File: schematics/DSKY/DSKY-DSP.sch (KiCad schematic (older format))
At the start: 0 parts

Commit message: Add files via upload
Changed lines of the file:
@@
 Wire Bus Line
 	5000 3600 5850 3600
-Wire Wire Line
-	7200 4950 8450 4950
 Wire Bus Line
 	2950 3900 3950 3900
@@
 F9 "DA2[1..3]" I L 8450 2150 50
 F10 "DA3[1..3]" I L 8450 2300 50
-F11 "MODE1" I L 8450 4950 50
-F12 "ID2[0..4]" I L 8450 4650 50
-F13 "ID3[0..4]" I L 8450 4800 50
+F11 "ID2[0..4]" I L 8450 4650 50
+F12 "ID3[0..4]" I L 8450 4800 50
 $EndSheet
 $Sheet
@@
 F4 "WRITE1" O R 7200 5050 50
 F5 "RWD[0..12]" I R 7200 4150 50
-F6 "MODE1" O R 7200 4950 50
-F7 "OW[11..11]" I L 5850 4050 50
-F8 "ID2[0..4]" O R 7200 4650 50
-F9 "ID3[0..4]" O R 7200 4800 50
-F10 "BI[1..8]" I L 5850 4250 50
+F6 "OW[11..11]" I L 5850 4050 50
+F7 "ID2[0..4]" O R 7200 4650 50
+F8 "ID3[0..4]" O R 7200 4800 50
+F9 "BI[1..8]" I L 5850 4250 50
 $EndSheet
 Wire Bus Line

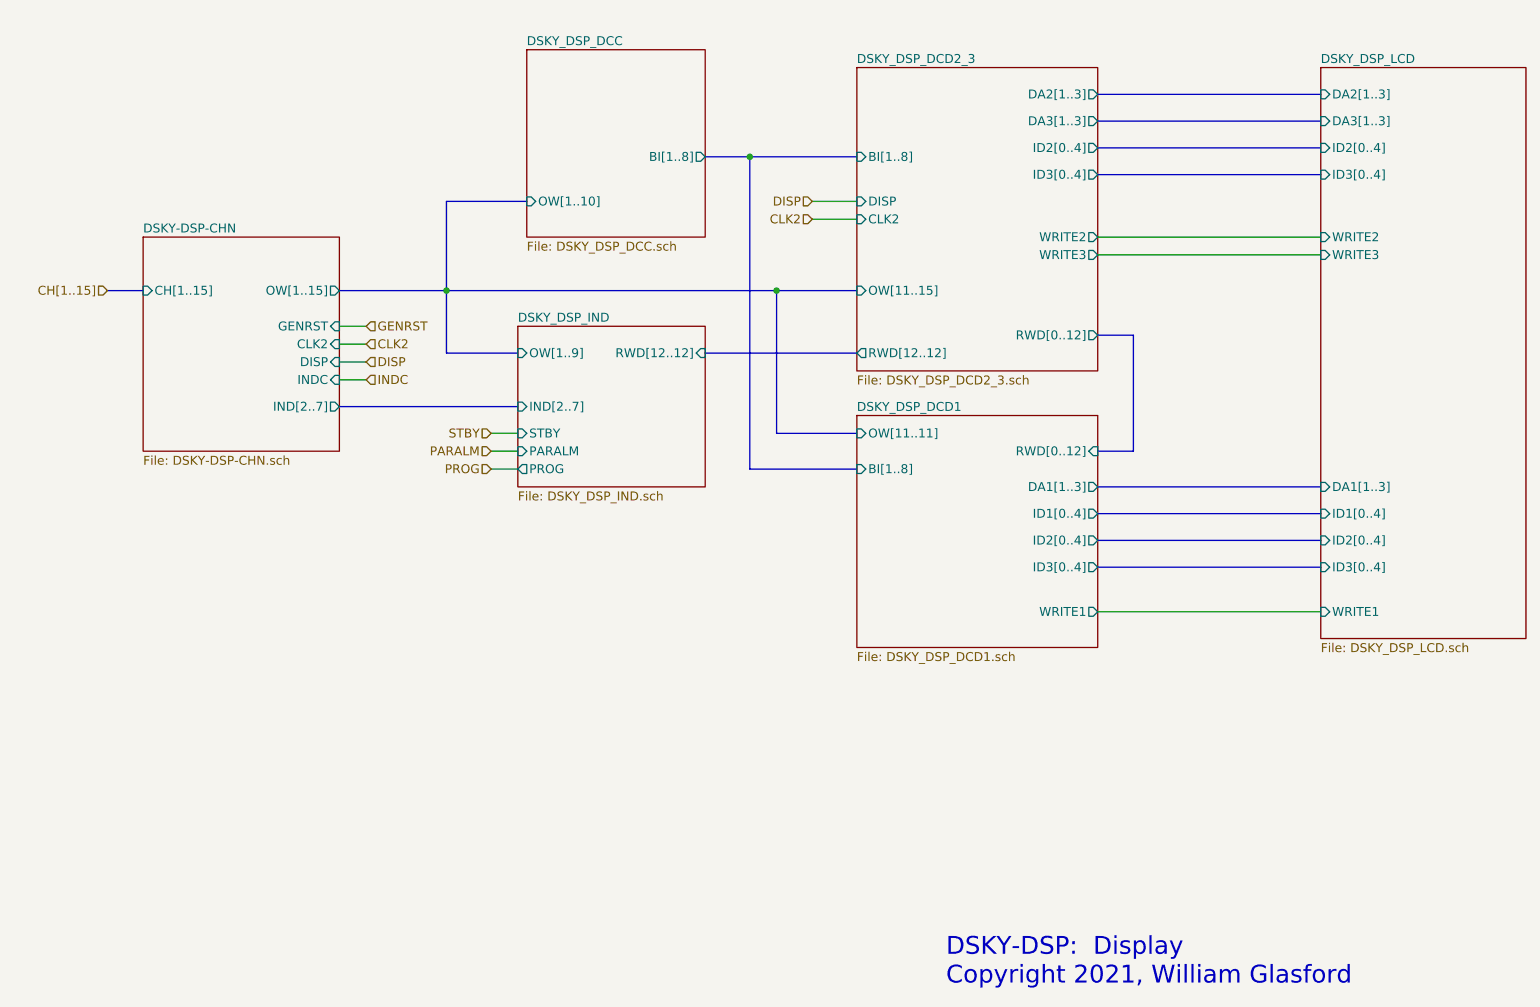
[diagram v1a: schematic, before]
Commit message: Minor tweaks to the display decoding logic.
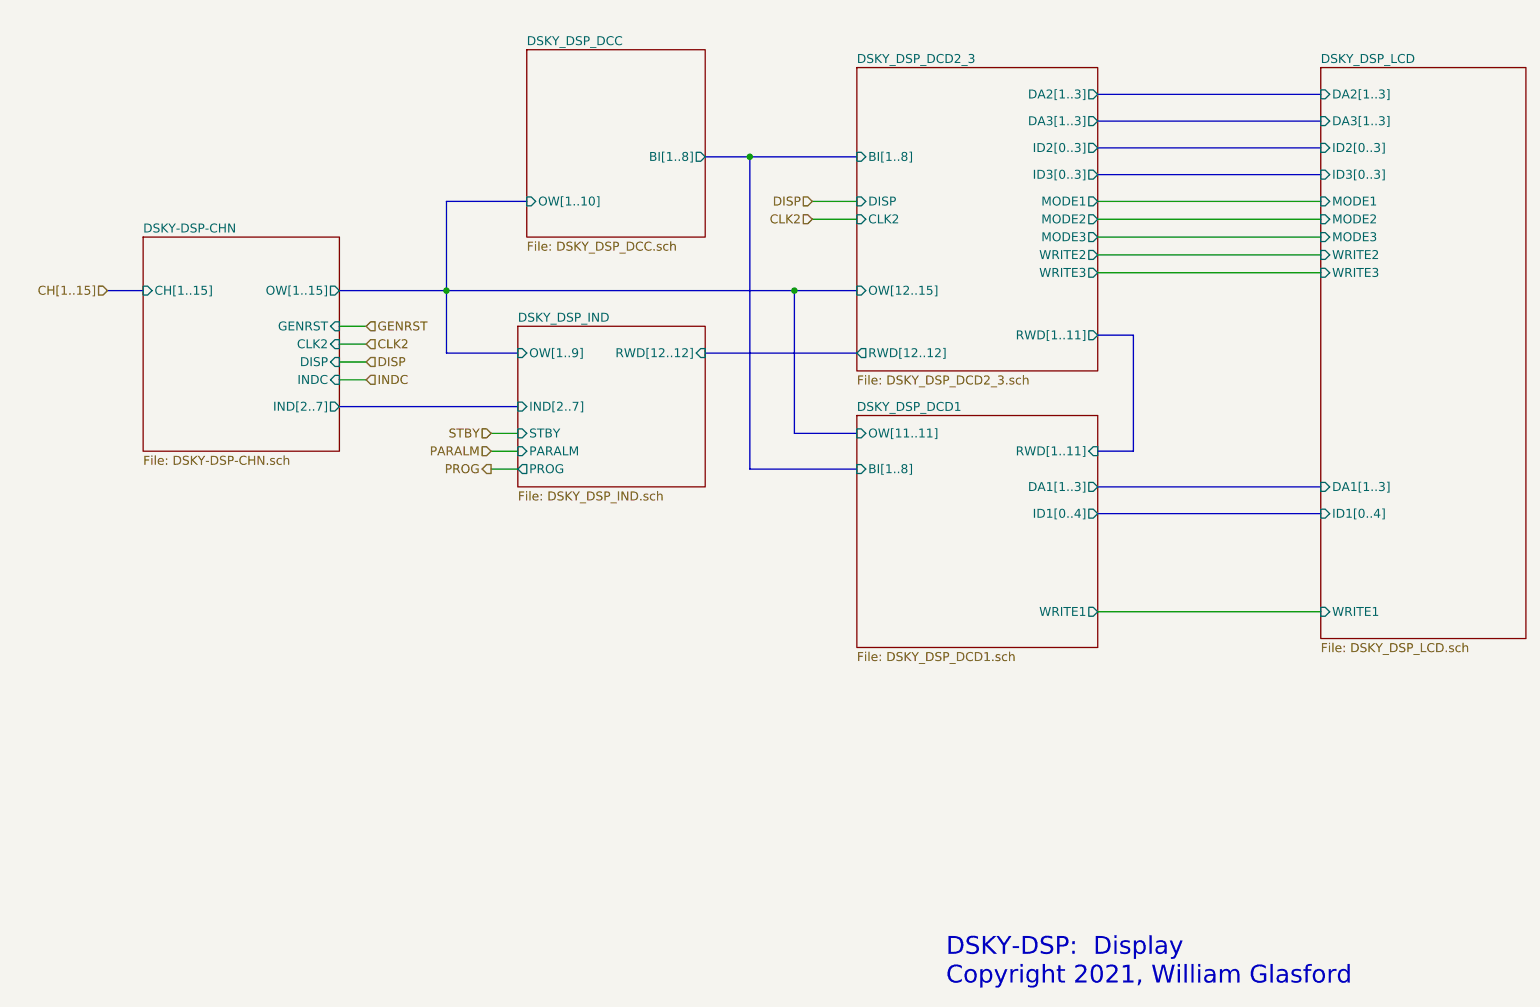
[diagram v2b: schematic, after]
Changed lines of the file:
@@
 	3550 3600 3950 3600
-Wire Bus Line
-	3550 3250 5400 3250
 Wire Bus Line
 	5000 2500 5250 2500
@@
 F1 "DSKY_DSP_DCD2_3.sch" 50
 F2 "BI[1..8]" I L 5850 2500 50
-F3 "OW[11..15]" I L 5850 3250 50
+F3 "OW[12..15]" I L 5850 3250 50
 F4 "DISP" I L 5850 2750 50
 F5 "CLK2" I L 5850 2850 50
@@
 F7 "DA2[1..3]" O R 7200 2150 50
 F8 "DA3[1..3]" O R 7200 2300 50
-F9 "ID2[0..4]" O R 7200 2450 50
-F10 "ID3[0..4]" O R 7200 2600 50
-F11 "WRITE2" O R 7200 2950 50
-F12 "WRITE3" O R 7200 3050 50
-F13 "RWD[0..12]" O R 7200 3500 50
+F9 "ID2[0..3]" O R 7200 2450 50
+F10 "ID3[0..3]" O R 7200 2600 50
+F11 "WRITE2" O R 7200 3050 50
+F12 "WRITE3" O R 7200 3150 50
+F13 "RWD[1..11]" O R 7200 3500 50
+F14 "MODE1" O R 7200 2750 50
+F15 "MODE2" O R 7200 2850 50
+F16 "MODE3" O R 7200 2950 50
 $EndSheet
 Wire Bus Line
@@
 F1 "DSKY_DSP_LCD.sch" 50
 F2 "DA1[1..3]" I L 8450 4350 50
-F3 "ID2[0..4]" I L 8450 2450 50
+F3 "ID2[0..3]" I L 8450 2450 50
 F4 "WRITE1" I L 8450 5050 50
-F5 "WRITE2" I L 8450 2950 50
-F6 "WRITE3" I L 8450 3050 50
+F5 "WRITE2" I L 8450 3050 50
+F6 "WRITE3" I L 8450 3150 50
 F7 "ID1[0..4]" I L 8450 4500 50
-F8 "ID3[0..4]" I L 8450 2600 50
+F8 "ID3[0..3]" I L 8450 2600 50
 F9 "DA2[1..3]" I L 8450 2150 50
 F10 "DA3[1..3]" I L 8450 2300 50
-F11 "ID2[0..4]" I L 8450 4650 50
-F12 "ID3[0..4]" I L 8450 4800 50
+F11 "MODE1" I L 8450 2750 50
+F12 "MODE2" I L 8450 2850 50
+F13 "MODE3" I L 8450 2950 50
 $EndSheet
 $Sheet
@@
 F3 "ID1[0..4]" O R 7200 4500 50
 F4 "WRITE1" O R 7200 5050 50
-F5 "RWD[0..12]" I R 7200 4150 50
-F6 "OW[11..11]" I L 5850 4050 50
-F7 "ID2[0..4]" O R 7200 4650 50
-F8 "ID3[0..4]" O R 7200 4800 50
-F9 "BI[1..8]" I L 5850 4250 50
+F5 "RWD[1..11]" I R 7200 4150 50
+F6 "BI[1..8]" I L 5850 4250 50
+F7 "OW[11..11]" I L 5850 4050 50
 $EndSheet
-Wire Bus Line
-	5850 4050 5400 4050
-Wire Bus Line
-	5400 4050 5400 3250
-Connection ~ 5400 3250
-Wire Bus Line
-	5400 3250 5850 3250
-Wire Bus Line
-	7200 4800 8450 4800
-Wire Bus Line
-	7200 4650 8450 4650
 Wire Bus Line
 	5850 4250 5250 4250
@@
 Wire Wire Line
 	3950 4250 3800 4250
-Text HLabel 3800 4250 0    50   Input ~ 0
+Text HLabel 3800 4250 0    50   Output ~ 0
 PROG
+Wire Wire Line
+	7200 2750 8450 2750
+Wire Wire Line
+	7200 2850 8450 2850
+Wire Wire Line
+	7200 3150 8450 3150
+Wire Bus Line
+	3550 3250 5500 3250
+Wire Bus Line
+	5500 3250 5500 4050
+Wire Bus Line
+	5500 4050 5850 4050
+Connection ~ 5500 3250
+Wire Bus Line
+	5500 3250 5850 3250
 $EndSCHEMATC

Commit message: Simplified...
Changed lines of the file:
@@
 F1 "DSKY_DSP_DCC.sch" 50
 F2 "OW[1..10]" I L 4000 2750 50
-F3 "BI[1..8]" O R 5000 2500 50
+F3 "ID2[0..3]" O R 5000 2350 50
+F4 "ID3[0..3]" O R 5000 2500 50
 $EndSheet
 Text HLabel 5600 2750 0    50   Input ~ 0
@@
 	3550 3600 3950 3600
 Wire Bus Line
-	5000 2500 5250 2500
+	5000 2500 5150 2500
 Wire Bus Line
 	7200 4350 8450 4350
-Wire Bus Line
-	7200 2150 8450 2150
 Wire Bus Line
 	2950 3250 3550 3250
@@
 INDC
 Wire Bus Line
-	7200 2300 8450 2300
-Wire Bus Line
 	7200 4500 8450 4500
 Connection ~ 3550 3250
@@
 F0 "DSKY_DSP_DCD2_3" 50
 F1 "DSKY_DSP_DCD2_3.sch" 50
-F2 "BI[1..8]" I L 5850 2500 50
-F3 "OW[12..15]" I L 5850 3250 50
-F4 "DISP" I L 5850 2750 50
-F5 "CLK2" I L 5850 2850 50
-F6 "RWD[12..12]" O L 5850 3600 50
-F7 "DA2[1..3]" O R 7200 2150 50
-F8 "DA3[1..3]" O R 7200 2300 50
-F9 "ID2[0..3]" O R 7200 2450 50
-F10 "ID3[0..3]" O R 7200 2600 50
-F11 "WRITE2" O R 7200 3050 50
-F12 "WRITE3" O R 7200 3150 50
-F13 "RWD[1..11]" O R 7200 3500 50
-F14 "MODE1" O R 7200 2750 50
-F15 "MODE2" O R 7200 2850 50
-F16 "MODE3" O R 7200 2950 50
+F2 "OW[12..15]" I L 5850 3250 50
+F3 "DISP" I L 5850 2750 50
+F4 "CLK2" I L 5850 2850 50
+F5 "RWD[12..12]" O L 5850 3600 50
+F6 "DA2[1..3]" O R 7200 2450 50
+F7 "DA3[1..3]" O R 7200 2600 50
+F8 "WRITE2" O R 7200 3050 50
+F9 "WRITE3" O R 7200 3150 50
+F10 "RWD[1..11]" O R 7200 3500 50
+F11 "MODE1" O R 7200 2750 50
+F12 "MODE2" O R 7200 2850 50
+F13 "MODE3" O R 7200 2950 50
 $EndSheet
 Wire Bus Line
@@
 F1 "DSKY_DSP_LCD.sch" 50
 F2 "DA1[1..3]" I L 8450 4350 50
-F3 "ID2[0..3]" I L 8450 2450 50
+F3 "ID2[0..3]" I L 8450 2150 50
 F4 "WRITE1" I L 8450 5050 50
 F5 "WRITE2" I L 8450 3050 50
 F6 "WRITE3" I L 8450 3150 50
 F7 "ID1[0..4]" I L 8450 4500 50
-F8 "ID3[0..3]" I L 8450 2600 50
-F9 "DA2[1..3]" I L 8450 2150 50
-F10 "DA3[1..3]" I L 8450 2300 50
+F8 "ID3[0..3]" I L 8450 2300 50
+F9 "DA2[1..3]" I L 8450 2450 50
+F10 "DA3[1..3]" I L 8450 2600 50
 F11 "MODE1" I L 8450 2750 50
 F12 "MODE2" I L 8450 2850 50
@@
 F4 "WRITE1" O R 7200 5050 50
 F5 "RWD[1..11]" I R 7200 4150 50
-F6 "BI[1..8]" I L 5850 4250 50
+F6 "ID3[0..3]" I L 5850 4300 50
 F7 "OW[11..11]" I L 5850 4050 50
-$EndSheet
-Wire Bus Line
-	5850 4250 5250 4250
-Wire Bus Line
-	5250 4250 5250 2500
-Connection ~ 5250 2500
-Wire Bus Line
-	5250 2500 5850 2500
+F8 "CLK2" I L 5850 4450 50
+F9 "ID2[0..3]" I L 5850 4200 50
+$EndSheet
+Wire Bus Line
+	5150 4300 5150 2500
 Text Notes 6350 7150 0    100  ~ 0
 DSKY-DSP:  Display \nCopyright 2021, William Glasford
@@
 Wire Bus Line
 	5500 3250 5850 3250
+Wire Wire Line
+	5850 4450 5600 4450
+Text HLabel 5600 4450 0    50   Input ~ 0
+CLK2
+Wire Bus Line
+	5150 4300 5850 4300
+Wire Bus Line
+	5000 2350 5300 2350
+Wire Bus Line
+	5300 2350 5300 4200
+Wire Bus Line
+	5300 4200 5850 4200
+Wire Bus Line
+	8450 2300 7600 2300
+Wire Bus Line
+	7600 2300 7600 1850
+Wire Bus Line
+	5150 1850 5150 2500
+Wire Bus Line
+	5150 1850 7600 1850
+Connection ~ 5150 2500
+Wire Bus Line
+	5300 1700 5300 2350
+Connection ~ 5300 2350
+Wire Bus Line
+	8450 2150 7750 2150
+Wire Bus Line
+	7750 2150 7750 1700
+Wire Bus Line
+	5300 1700 7750 1700
 $EndSCHEMATC

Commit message: Minor tweaks.
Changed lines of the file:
@@
 F1 "DSKY_DSP_IND.sch" 50
 F2 "RWD[12..12]" I R 5000 3600 50
-F3 "OW[1..9]" I L 3950 3600 50
+F3 "OW[3..9]" I L 3950 3600 50
 F4 "STBY" I L 3950 4050 50
 F5 "PARALM" I L 3950 4150 50
@@
 Wire Bus Line
 	7400 4150 7200 4150
-$Sheet
-S 5850 2000 1350 1700
-U 637944C1
-F0 "DSKY_DSP_DCD2_3" 50
-F1 "DSKY_DSP_DCD2_3.sch" 50
-F2 "OW[12..15]" I L 5850 3250 50
-F3 "DISP" I L 5850 2750 50
-F4 "CLK2" I L 5850 2850 50
-F5 "RWD[12..12]" O L 5850 3600 50
-F6 "DA2[1..3]" O R 7200 2450 50
-F7 "DA3[1..3]" O R 7200 2600 50
-F8 "WRITE2" O R 7200 3050 50
-F9 "WRITE3" O R 7200 3150 50
-F10 "RWD[1..11]" O R 7200 3500 50
-F11 "MODE1" O R 7200 2750 50
-F12 "MODE2" O R 7200 2850 50
-F13 "MODE3" O R 7200 2950 50
-$EndSheet
 Wire Bus Line
 	5000 3600 5850 3600
 Wire Bus Line
 	2950 3900 3950 3900
-$Sheet
-S 8450 2000 1150 3200
-U 63794556
-F0 "DSKY_DSP_LCD" 50
-F1 "DSKY_DSP_LCD.sch" 50
-F2 "DA1[1..3]" I L 8450 4350 50
-F3 "ID2[0..3]" I L 8450 2150 50
-F4 "WRITE1" I L 8450 5050 50
-F5 "WRITE2" I L 8450 3050 50
-F6 "WRITE3" I L 8450 3150 50
-F7 "ID1[0..4]" I L 8450 4500 50
-F8 "ID3[0..3]" I L 8450 2300 50
-F9 "DA2[1..3]" I L 8450 2450 50
-F10 "DA3[1..3]" I L 8450 2600 50
-F11 "MODE1" I L 8450 2750 50
-F12 "MODE2" I L 8450 2850 50
-F13 "MODE3" I L 8450 2950 50
-$EndSheet
 $Sheet
 S 5850 3950 1350 1300
@@
 Wire Bus Line
 	5300 1700 7750 1700
+$Sheet
+S 8450 2000 1150 3200
+U 63794556
+F0 "DSKY_DSP_LCD" 50
+F1 "DSKY_DSP_LCD.sch" 50
+F2 "DA1[1..3]" I L 8450 4350 50
+F3 "ID2[0..3]" I L 8450 2150 50
+F4 "WRITE1" I L 8450 5050 50
+F5 "WRITE2" I L 8450 3050 50
+F6 "WRITE3" I L 8450 3150 50
+F7 "ID1[0..4]" I L 8450 4500 50
+F8 "ID3[0..3]" I L 8450 2300 50
+F9 "DA2[1..3]" I L 8450 2450 50
+F10 "DA3[1..3]" I L 8450 2600 50
+F11 "MODE1" I L 8450 2750 50
+F12 "MODE2" I L 8450 2850 50
+F13 "MODE3" I L 8450 2950 50
+$EndSheet
+$Sheet
+S 5850 2000 1350 1700
+U 637944C1
+F0 "DSKY_DSP_DCD2_3" 50
+F1 "DSKY_DSP_DCD2_3.sch" 50
+F2 "OW[12..15]" I L 5850 3250 50
+F3 "DISP" I L 5850 2750 50
+F4 "CLK2" I L 5850 2850 50
+F5 "RWD[12..12]" O L 5850 3600 50
+F6 "DA2[1..3]" O R 7200 2450 50
+F7 "DA3[1..3]" O R 7200 2600 50
+F8 "WRITE2" O R 7200 3050 50
+F9 "WRITE3" O R 7200 3150 50
+F10 "RWD[1..11]" O R 7200 3500 50
+F11 "MODE1" O R 7200 2750 50
+F12 "MODE2" O R 7200 2850 50
+F13 "MODE3" O R 7200 2950 50
+$EndSheet
 $EndSCHEMATC

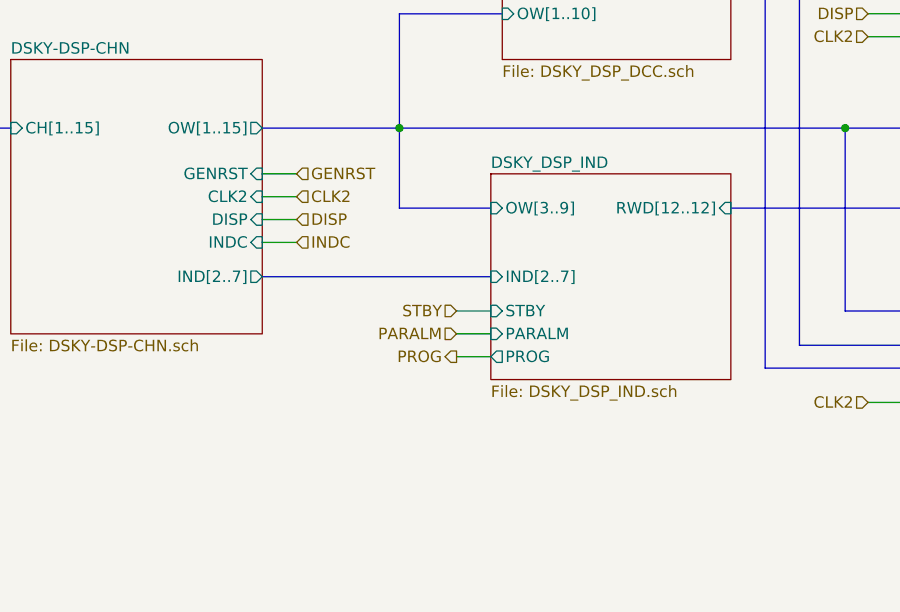
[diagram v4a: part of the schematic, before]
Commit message: Simplified reset lines.
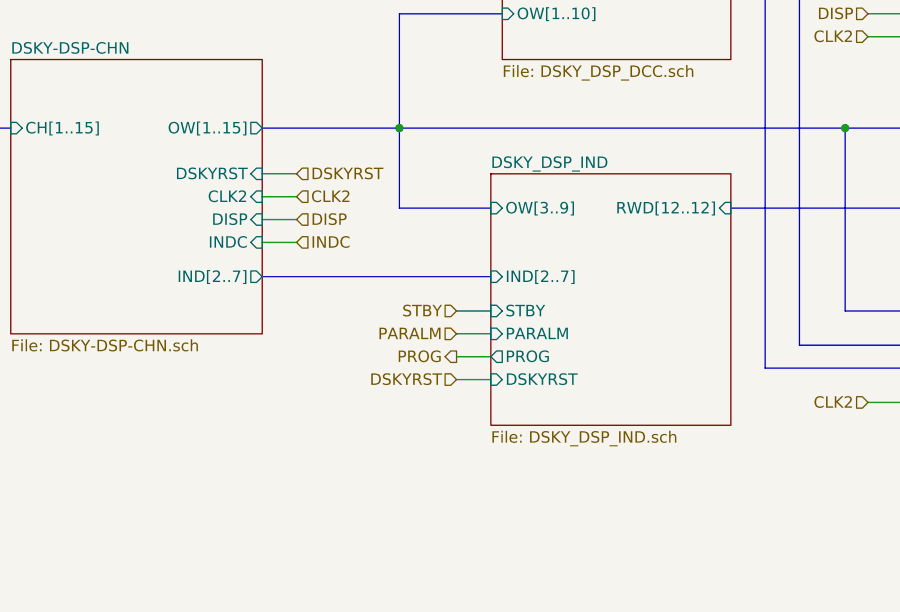
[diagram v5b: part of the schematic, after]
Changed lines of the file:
@@
 F3 "IND[2..7]" O R 2950 3900 50
 F4 "CH[1..15]" I L 1850 3250 50
-F5 "GENRST" I R 2950 3450 50
+F5 "DSKYRST" I R 2950 3450 50
 F6 "CLK2" I R 2950 3550 50
 F7 "DISP" I R 2950 3650 50
@@
 PARALM
 $Sheet
-S 3950 3450 1050 900
+S 3950 3450 1050 1100
 U 68A00B2E
 F0 "DSKY_DSP_IND" 50
@@
 F6 "IND[2..7]" I L 3950 3900 50
 F7 "PROG" O L 3950 4250 50
+F8 "DSKYRST" I L 3950 4350 50
 $EndSheet
 Wire Bus Line
@@
 	3100 3550 2950 3550
 Text HLabel 3100 3450 2    50   Input ~ 0
-GENRST
+DSKYRST
 Text HLabel 3100 3550 2    50   Input ~ 0
 CLK2
@@
 F13 "MODE3" O R 7200 2950 50
 $EndSheet
+Text HLabel 3800 4350 0    50   Input ~ 0
+DSKYRST
+Wire Wire Line
+	3800 4350 3950 4350
 $EndSCHEMATC

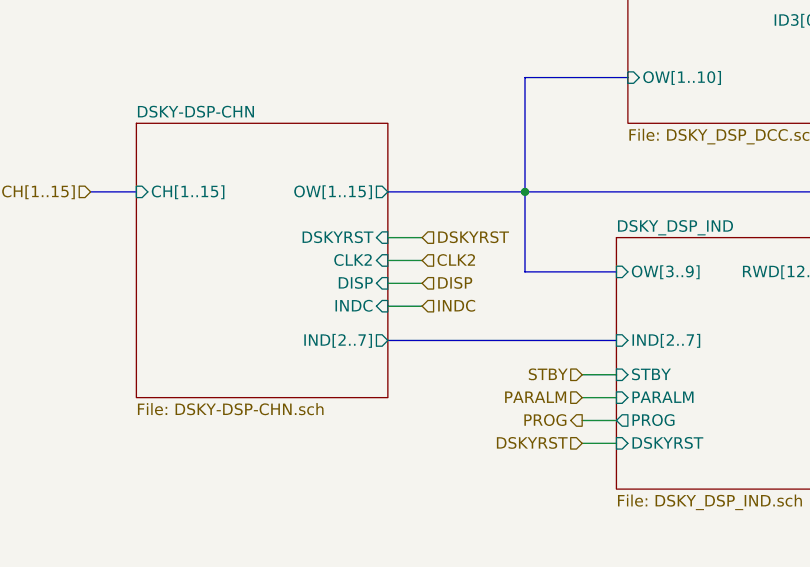
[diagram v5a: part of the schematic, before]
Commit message: Cleaned up clock logic.
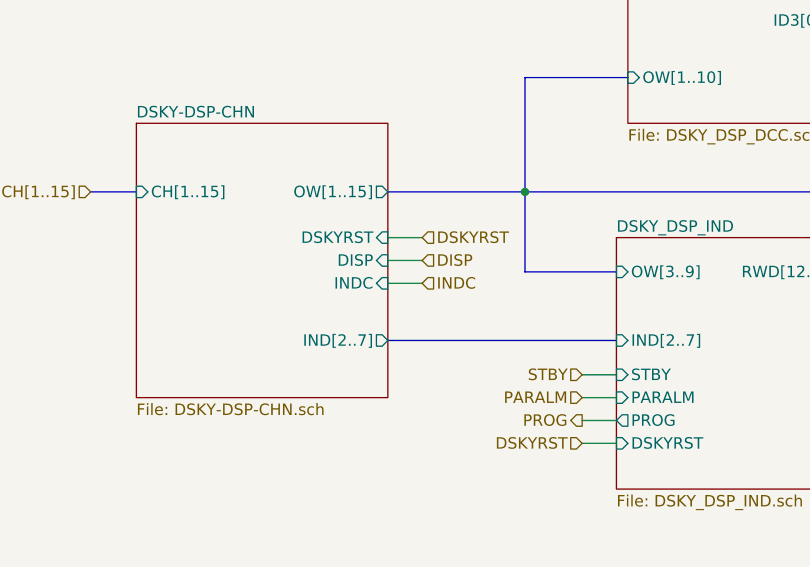
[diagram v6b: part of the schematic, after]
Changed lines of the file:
@@
 F4 "CH[1..15]" I L 1850 3250 50
 F5 "DSKYRST" I R 2950 3450 50
-F6 "CLK2" I R 2950 3550 50
-F7 "DISP" I R 2950 3650 50
-F8 "INDC" I R 2950 3750 50
+F6 "DISP" I R 2950 3550 50
+F7 "INDC" I R 2950 3650 50
 $EndSheet
 Text HLabel 3800 4050 0    50   Input ~ 0
@@
 Text HLabel 3100 3450 2    50   Input ~ 0
 DSKYRST
-Text HLabel 3100 3550 2    50   Input ~ 0
-CLK2
 Wire Wire Line
 	2950 3450 3100 3450
 Wire Wire Line
 	3100 3650 2950 3650
+Text HLabel 3100 3550 2    50   Input ~ 0
+DISP
 Text HLabel 3100 3650 2    50   Input ~ 0
-DISP
-Wire Wire Line
-	3100 3750 2950 3750
-Text HLabel 3100 3750 2    50   Input ~ 0
 INDC
 Wire Bus Line
